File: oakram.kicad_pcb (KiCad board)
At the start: 2 copper layers, 10 parts, among them U1 IS41C16105C, U2 IS41C16105C, X1 ZIP40, X2 ZIP40

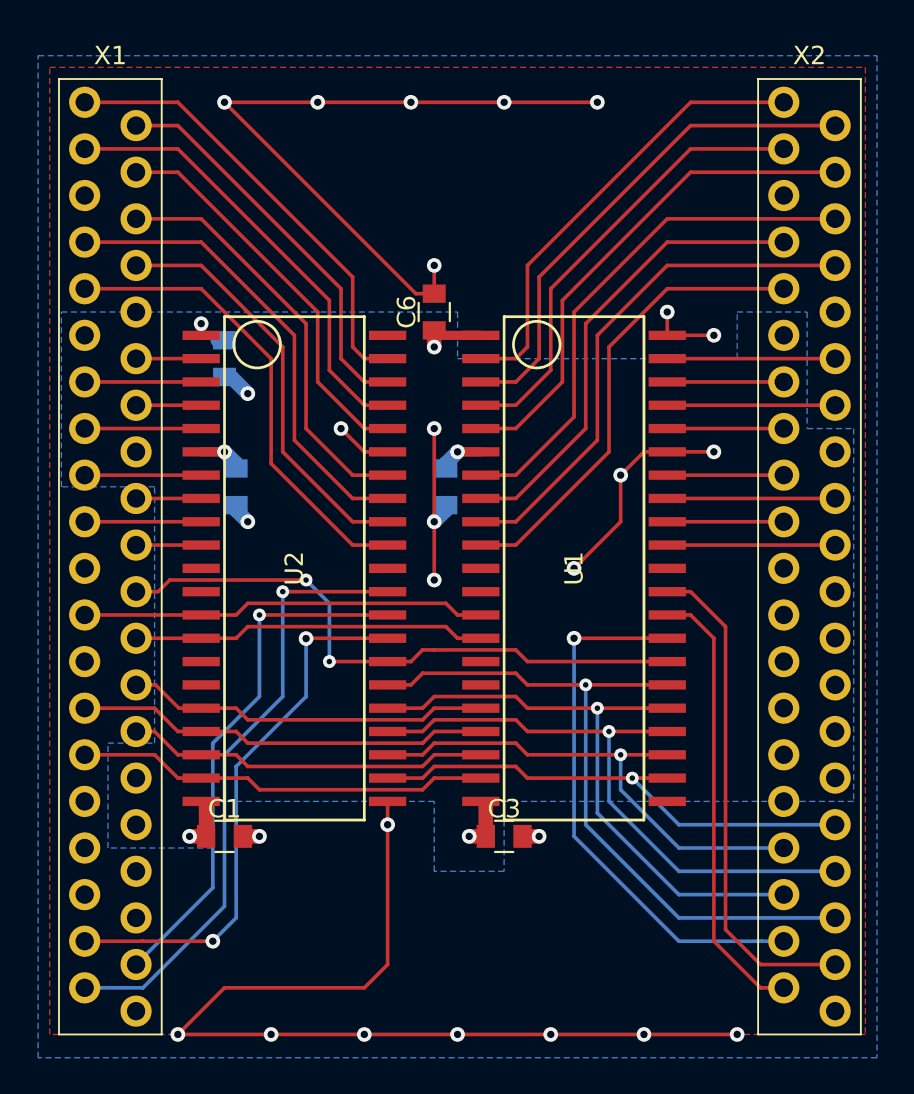
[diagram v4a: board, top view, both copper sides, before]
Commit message: Added elcap
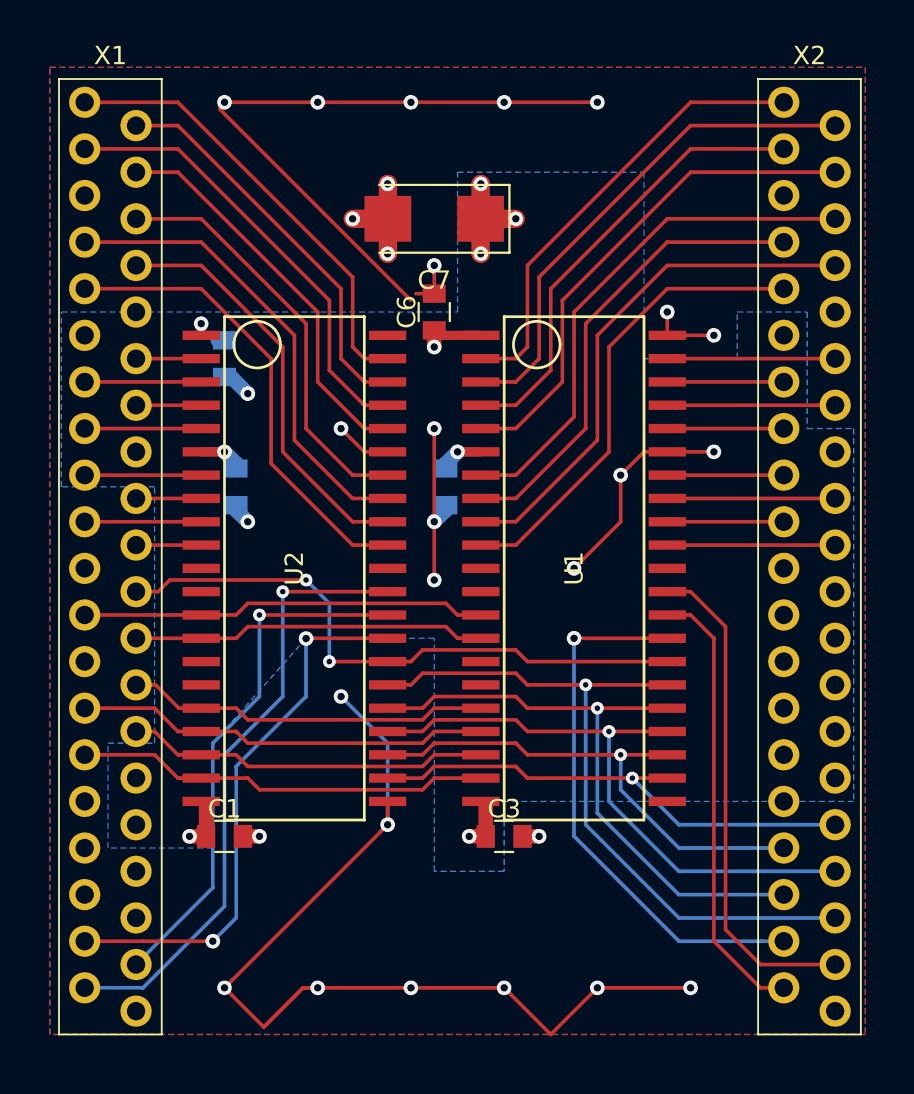
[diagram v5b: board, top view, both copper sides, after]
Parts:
- added C7: 47u 16V, Capacitors_Tantalum_SMD:CP_Tantalum_Case-C_EIA-6032-28_Reflow, F.Cu at (141.0, 82.5)
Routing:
- net VSS: track 123.4 -> 131.2 mm, vias 27 -> 30
- net VCC: track 15.3 -> 21.0 mm, vias 6 -> 9
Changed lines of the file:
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@@
     (thickness 1.6)
     (drawings 4)
-    (tracks 331)
+    (tracks 355)
     (zones 0)
-    (modules 10)
+    (modules 11)
     (nets 74)
   )
@@
       (net 56 VSS))
     (model Capacitors_SMD.3dshapes/C_0805.wrl
+      (at (xyz 0 0 0))
+      (scale (xyz 1 1 1))
+      (rotate (xyz 0 0 0))
+    )
+  )
+  (module Capacitors_Tantalum_SMD:CP_Tantalum_Case-C_EIA-6032-28_Reflow (layer F.Cu)
+    (at 140.97 82.55 180)
+    (descr "Tantalum capacitor, Case C, EIA 6032-28, 6.0x3.2x2.5mm, Reflow soldering footprint")
+    (tags "capacitor tantalum smd")
+    (attr smd)
+    (fp_text reference C7 (at 0 -3.35 180) (layer F.SilkS)
+      (effects (font (size 1 1) (thickness 0.15)))
+    )
+    (fp_text value "47u 16V" (at 0 3.35 180) (layer F.Fab)
+      (effects (font (size 1 1) (thickness 0.15)))
+    )
+    (fp_line (start -4.1 -1.85) (end -4.1 1.85) (layer F.SilkS) (width 0.12))
+    (fp_line (start -4.1 1.85) (end 3 1.85) (layer F.SilkS) (width 0.12))
+    (fp_line (start -4.1 -1.85) (end 3 -1.85) (layer F.SilkS) (width 0.12))
+    (fp_line (start -2.1 -1.6) (end -2.1 1.6) (layer F.Fab) (width 0.1))
+    (fp_line (start -2.4 -1.6) (end -2.4 1.6) (layer F.Fab) (width 0.1))
+    (fp_line (start 3 -1.6) (end -3 -1.6) (layer F.Fab) (width 0.1))
+    (fp_line (start 3 1.6) (end 3 -1.6) (layer F.Fab) (width 0.1))
+    (fp_line (start -3 1.6) (end 3 1.6) (layer F.Fab) (width 0.1))
+    (fp_line (start -3 -1.6) (end -3 1.6) (layer F.Fab) (width 0.1))
+    (fp_line (start 4.2 -2) (end -4.2 -2) (layer F.CrtYd) (width 0.05))
+    (fp_line (start 4.2 2) (end 4.2 -2) (layer F.CrtYd) (width 0.05))
+    (fp_line (start -4.2 2) (end 4.2 2) (layer F.CrtYd) (width 0.05))
+    (fp_line (start -4.2 -2) (end -4.2 2) (layer F.CrtYd) (width 0.05))
+    (fp_text user %R (at 0 0 180) (layer F.Fab)
+      (effects (font (size 1 1) (thickness 0.15)))
+    )
+    (pad 2 smd rect (at 2.525 0 180) (size 2.55 2.5) (layers F.Cu F.Paste F.Mask)
+      (net 56 VSS))
+    (pad 1 smd rect (at -2.525 0 180) (size 2.55 2.5) (layers F.Cu F.Paste F.Mask)
+      (net 57 VCC))
+    (model Capacitors_Tantalum_SMD.3dshapes/CP_Tantalum_Case-C_EIA-6032-28.wrl
       (at (xyz 0 0 0))
       (scale (xyz 1 1 1))
@@
   (segment (start 146.05 85.09) (end 154.94 76.2) (width 0.2) (layer F.Cu) (net 55))
   (segment (start 154.94 76.2) (end 160.02 76.2) (width 0.2) (layer F.Cu) (net 55))
+  (segment (start 138.43 115.57) (end 138.43 111.125) (width 0.2) (layer B.Cu) (net 56))
+  (segment (start 138.43 111.125) (end 135.89 108.585) (width 0.2) (layer B.Cu) (net 56))
+  (via (at 135.89 108.585) (size 0.8) (drill 0.4) (layers F.Cu B.Cu) (net 56))
+  (segment (start 149.86 124.46) (end 154.94 124.46) (width 0.2) (layer F.Cu) (net 56))
+  (via (at 154.94 124.46) (size 0.8) (drill 0.4) (layers F.Cu B.Cu) (net 56))
+  (segment (start 147.32 127) (end 149.86 124.46) (width 0.2) (layer F.Cu) (net 56))
+  (via (at 149.86 124.46) (size 0.8) (drill 0.4) (layers F.Cu B.Cu) (net 56))
+  (segment (start 144.78 124.46) (end 147.32 127) (width 0.2) (layer F.Cu) (net 56))
+  (segment (start 139.7 124.46) (end 144.78 124.46) (width 0.2) (layer F.Cu) (net 56))
+  (via (at 144.78 124.46) (size 0.8) (drill 0.4) (layers F.Cu B.Cu) (net 56))
+  (segment (start 134.62 124.46) (end 139.7 124.46) (width 0.2) (layer F.Cu) (net 56))
+  (via (at 139.7 124.46) (size 0.8) (drill 0.4) (layers F.Cu B.Cu) (net 56))
+  (via (at 134.62 124.46) (size 0.8) (drill 0.4) (layers F.Cu B.Cu) (net 56))
+  (segment (start 134.054315 124.46) (end 134.62 124.46) (width 0.2) (layer F.Cu) (net 56))
+  (segment (start 131.680001 126.600001) (end 133.820002 124.46) (width 0.2) (layer F.Cu) (net 56))
+  (segment (start 133.82 124.46) (end 134.054315 124.46) (width 0.2) (layer F.Cu) (net 56))
+  (segment (start 131.680001 126.599999) (end 133.82 124.46) (width 0.2) (layer F.Cu) (net 56))
+  (segment (start 131.680001 126.599999) (end 131.680001 126.600001) (width 0.2) (layer F.Cu) (net 56))
+  (segment (start 129.54 124.459998) (end 129.939999 124.859999) (width 0.2) (layer F.Cu) (net 56))
+  (segment (start 133.820002 124.46) (end 134.054315 124.46) (width 0.2) (layer F.Cu) (net 56))
+  (segment (start 129.939999 124.859999) (end 131.680001 126.600001) (width 0.2) (layer F.Cu) (net 56))
+  (segment (start 138.029999 115.969999) (end 129.939999 124.059999) (width 0.2) (layer F.Cu) (net 56))
+  (segment (start 138.43 115.57) (end 138.029999 115.969999) (width 0.2) (layer F.Cu) (net 56))
+  (segment (start 129.939999 124.059999) (end 129.54 124.459998) (width 0.2) (layer F.Cu) (net 56))
+  (via (at 129.54 124.459998) (size 0.8) (drill 0.4) (layers F.Cu B.Cu) (net 56))
+  (segment (start 138.445 82.55) (end 138.445 84.44) (width 1) (layer F.Cu) (net 56))
+  (segment (start 138.445 84.44) (end 138.43 84.455) (width 1) (layer F.Cu) (net 56))
+  (via (at 138.43 84.455) (size 0.8) (drill 0.4) (layers F.Cu B.Cu) (net 56))
+  (segment (start 138.445 82.55) (end 138.445 80.66) (width 1) (layer F.Cu) (net 56))
+  (segment (start 138.445 80.66) (end 138.43 80.645) (width 1) (layer F.Cu) (net 56))
+  (via (at 138.43 80.645) (size 0.8) (drill 0.4) (layers F.Cu B.Cu) (net 56))
+  (segment (start 138.445 82.55) (end 136.525 82.55) (width 1) (layer F.Cu) (net 56))
+  (via (at 136.525 82.55) (size 0.8) (drill 0.4) (layers F.Cu B.Cu) (net 56))
   (segment (start 144.78 76.2) (end 149.86 76.2) (width 0.2) (layer F.Cu) (net 56))
   (via (at 149.86 76.2) (size 0.8) (drill 0.4) (layers F.Cu B.Cu) (net 56))
@@
   (via (at 134.62 76.2) (size 0.8) (drill 0.4) (layers F.Cu B.Cu) (net 56))
   (segment (start 140.97 86.63) (end 139.97 86.63) (width 0.2) (layer F.Cu) (net 56))
-  (segment (start 139.97 86.63) (end 129.54 76.2) (width 0.2) (layer F.Cu) (net 56))
+  (segment (start 139.7 86.995) (end 129.27 76.565) (width 0.2) (layer F.Cu) (net 56))
   (via (at 129.54 76.2) (size 0.8) (drill 0.4) (layers F.Cu B.Cu) (net 56))
-  (segment (start 152.4 127) (end 157.48 127) (width 0.2) (layer F.Cu) (net 56))
-  (via (at 157.48 127) (size 0.8) (drill 0.4) (layers F.Cu B.Cu) (net 56))
-  (segment (start 147.32 127) (end 152.4 127) (width 0.2) (layer F.Cu) (net 56))
-  (via (at 152.4 127) (size 0.8) (drill 0.4) (layers F.Cu B.Cu) (net 56))
-  (segment (start 142.24 127) (end 147.32 127) (width 0.2) (layer F.Cu) (net 56))
-  (via (at 147.32 127) (size 0.8) (drill 0.4) (layers F.Cu B.Cu) (net 56))
-  (segment (start 137.16 127) (end 142.24 127) (width 0.2) (layer F.Cu) (net 56))
-  (via (at 142.24 127) (size 0.8) (drill 0.4) (layers F.Cu B.Cu) (net 56))
-  (segment (start 132.08 127) (end 137.16 127) (width 0.2) (layer F.Cu) (net 56))
-  (via (at 137.16 127) (size 0.8) (drill 0.4) (layers F.Cu B.Cu) (net 56))
-  (segment (start 127 127) (end 132.08 127) (width 0.2) (layer F.Cu) (net 56))
-  (via (at 132.08 127) (size 0.8) (drill 0.4) (layers F.Cu B.Cu) (net 56))
-  (segment (start 137.16 124.46) (end 129.54 124.46) (width 0.2) (layer F.Cu) (net 56))
-  (segment (start 129.54 124.46) (end 127 127) (width 0.2) (layer F.Cu) (net 56))
-  (via (at 127 127) (size 0.8) (drill 0.4) (layers F.Cu B.Cu) (net 56))
-  (segment (start 138.43 123.19) (end 137.16 124.46) (width 0.2) (layer F.Cu) (net 56))
-  (segment (start 138.43 115.57) (end 138.43 123.19) (width 0.2) (layer F.Cu) (net 56))
   (segment (start 140.97 99.06) (end 140.97 102.235) (width 0.2) (layer F.Cu) (net 56))
   (via (at 140.97 102.235) (size 0.8) (drill 0.4) (layers F.Cu B.Cu) (net 56))
@@
   (segment (start 130.54 116.205) (end 131.445 116.205) (width 0.8) (layer F.Cu) (net 56))
   (via (at 131.445 116.205) (size 0.8) (drill 0.4) (layers F.Cu B.Cu) (net 56))
+  (segment (start 143.495 82.55) (end 143.495 80.66) (width 1) (layer F.Cu) (net 57))
+  (segment (start 143.495 80.66) (end 143.51 80.645) (width 1) (layer F.Cu) (net 57))
+  (via (at 143.51 80.645) (size 0.8) (drill 0.4) (layers F.Cu B.Cu) (net 57))
+  (segment (start 143.495 82.55) (end 143.495 84.44) (width 1) (layer F.Cu) (net 57))
+  (segment (start 143.495 84.44) (end 143.51 84.455) (width 1) (layer F.Cu) (net 57))
+  (via (at 143.51 84.455) (size 0.8) (drill 0.4) (layers F.Cu B.Cu) (net 57))
+  (segment (start 143.495 82.55) (end 145.415 82.55) (width 1) (layer F.Cu) (net 57))
+  (via (at 145.415 82.55) (size 0.8) (drill 0.4) (layers F.Cu B.Cu) (net 57))
   (segment (start 140.97 88.63) (end 140.97 89.535) (width 0.8) (layer F.Cu) (net 57))
   (via (at 140.97 89.535) (size 0.8) (drill 0.4) (layers F.Cu B.Cu) (net 57))
@@
     (polygon
       (pts
-        (xy 119.38 73.66) (xy 165.1 73.66) (xy 165.1 128.27) (xy 119.38 128.27)
+        (xy 120.015 74.295) (xy 164.465 74.295) (xy 164.465 127) (xy 120.015 127)
       )
     )
@@
       (pts
         (xy 123.19 111.125) (xy 125.73 111.125) (xy 125.73 97.155) (xy 120.65 97.155) (xy 120.65 87.63)
-        (xy 142.24 87.63) (xy 142.24 90.17) (xy 157.48 90.17) (xy 157.48 87.63) (xy 161.29 87.63)
-        (xy 161.29 93.98) (xy 163.83 93.98) (xy 163.83 114.3) (xy 144.78 114.3) (xy 144.78 118.11)
-        (xy 140.97 118.11) (xy 140.97 114.3) (xy 128.905 114.3) (xy 128.905 116.84) (xy 123.19 116.84)
+        (xy 142.24 87.63) (xy 142.24 80.01) (xy 152.4 80.01) (xy 152.4 90.17) (xy 157.48 90.17)
+        (xy 157.48 87.63) (xy 161.29 87.63) (xy 161.29 93.98) (xy 163.83 93.98) (xy 163.83 114.3)
+        (xy 144.78 114.3) (xy 144.78 118.11) (xy 140.97 118.11) (xy 140.97 105.41) (xy 133.985 105.41)
+        (xy 128.905 111.125) (xy 128.905 116.84) (xy 123.19 116.84)
       )
     )

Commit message: Gerber release
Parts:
- moved X2 2.54 mm to (158.9, 100.3)
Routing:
- net VSS: track 131.2 -> 125.6 mm, vias 30 -> 29
- net /D28: track 28.4 -> 25.6 mm
- net /D25: track 27.7 -> 24.9 mm
- net /D23: track 9.15 -> 6.35 mm
- net /D18: track 9.15 -> 6.35 mm
- net /A6: track 33.5 -> 30.7 mm
- net /D29: track 25.6 -> 23.1 mm
- net /A7: track 33.5 -> 30.9 mm
- net /~OE: track 59.7 -> 57.2 mm
- net /D31: track 25.6 -> 23.1 mm
- net /D26: track 24.9 -> 22.4 mm
- net /D24: track 24.9 -> 22.4 mm
- net /D22: track 6.35 -> 3.81 mm
- net /D20: track 6.35 -> 3.81 mm
- net /D19: track 6.35 -> 3.81 mm
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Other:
- board outline added: 43.2 x 54 mm
- net class Default: trace_width 0.2 -> 0.25; via_dia 0.8 -> 0.7; via_drill 0.4 -> 0.3
- rule via_min_drill: 0.4 -> 0.3
- rule via_min_size: 0.8 -> 0.7
- board text added: "tnt23 2017"
